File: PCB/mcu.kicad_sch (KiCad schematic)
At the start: 14 parts, among them SW1 SW_Push, SW2 SW_Push, SW3 SW_Push, SW4 SW_Push, U3 COM-09032, Y1 Crystal_GND24

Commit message: Fix wiring
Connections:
- new net: H1.2 (PA1), R10.2, SW2.2
- new net: H1.1 (PA0), R9.2, SW1.2
- new net: H1.3 (PA2), R11.2, SW3.2
- new net: H1.4 (PA3), R12.2, SW4.2
- now unconnected: H1.5 (PA4), H1.6 (PA5)
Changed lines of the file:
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@@
   (junction (at 88.9 158.75) (diameter 0) (color 0 0 0 0)
   )
-  (junction (at 68.58 74.93) (diameter 0) (color 0 0 0 0)
-  )
   (junction (at 49.53 74.93) (diameter 0) (color 0 0 0 0)
   )
@@
   (junction (at 68.58 130.81) (diameter 0) (color 0 0 0 0)
   )
-  (junction (at 68.58 80.01) (diameter 0) (color 0 0 0 0)
-  )
   (junction (at 45.72 72.39) (diameter 0) (color 0 0 0 0)
   )
@@
   (junction (at 95.25 170.18) (diameter 0) (color 0 0 0 0)
   )
-  (junction (at 68.58 72.39) (diameter 0) (color 0 0 0 0)
-  )
   (junction (at 57.15 80.01) (diameter 0) (color 0 0 0 0)
   )
@@
   (junction (at 49.53 60.96) (diameter 0) (color 0 0 0 0)
   )
-  (junction (at 68.58 82.55) (diameter 0) (color 0 0 0 0)
-  )
   (junction (at 93.98 52.07) (diameter 0) (color 0 0 0 0)
   )
@@
   )
   (junction (at 83.82 52.07) (diameter 0) (color 0 0 0 0)
-  )
-  (junction (at 68.58 77.47) (diameter 0) (color 0 0 0 0)
   )
   (junction (at 129.54 72.39) (diameter 0) (color 0 0 0 0)
@@
     (stroke (width 0) (type default))
   )
-  (wire (pts (xy 68.58 77.47) (xy 68.58 80.01))
-    (stroke (width 0) (type default))
-  )
   (wire (pts (xy 53.34 60.96) (xy 57.15 60.96))
     (stroke (width 0) (type default))
@@
     (stroke (width 0) (type default))
   )
-  (wire (pts (xy 68.58 80.01) (xy 68.58 82.55))
-    (stroke (width 0) (type default))
-  )
   (wire (pts (xy 53.34 77.47) (xy 48.26 77.47))
     (stroke (width 0) (type default))
@@
     (stroke (width 0) (type default))
   )
-  (wire (pts (xy 68.58 82.55) (xy 68.58 85.09))
-    (stroke (width 0) (type default))
-  )
-  (wire (pts (xy 68.58 72.39) (xy 68.58 74.93))
-    (stroke (width 0) (type default))
-  )
   (wire (pts (xy 104.14 52.07) (xy 106.68 52.07))
     (stroke (width 0) (type default))
@@
     (stroke (width 0) (type default))
   )
-  (wire (pts (xy 68.58 74.93) (xy 68.58 77.47))
-    (stroke (width 0) (type default))
-  )

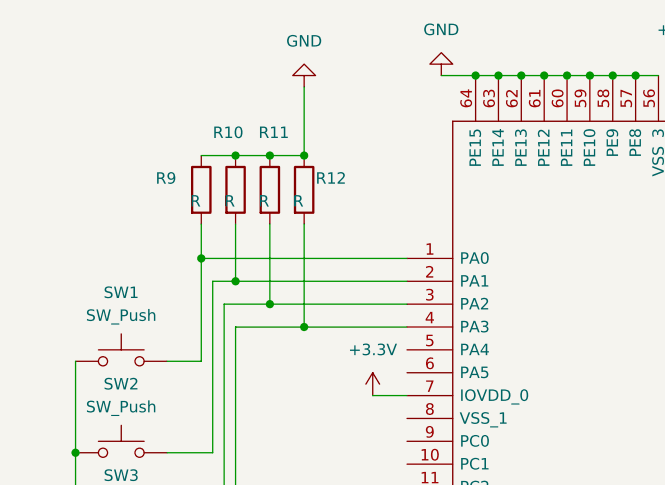
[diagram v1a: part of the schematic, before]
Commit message: Set resistor values
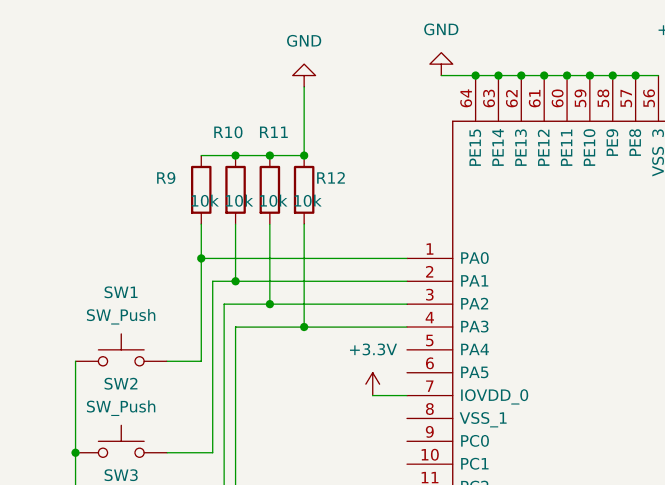
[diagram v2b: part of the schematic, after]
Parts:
- R10, R11, R12, R9: value R -> 10k
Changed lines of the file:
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@@
       (effects (font (size 1.27 1.27)) (justify left))
     )
-    (property "Value" "R" (at 48.26 66.04 0)
+    (property "Value" "10k" (at 48.26 66.04 0)
       (effects (font (size 1.27 1.27)) (justify left))
     )
@@
       (effects (font (size 1.27 1.27)) (justify left))
     )
-    (property "Value" "R" (at 44.45 66.04 0)
+    (property "Value" "10k" (at 44.45 66.04 0)
       (effects (font (size 1.27 1.27)) (justify left))
     )
@@
       (effects (font (size 1.27 1.27)) (justify left))
     )
-    (property "Value" "R" (at 55.88 66.04 0)
+    (property "Value" "10k" (at 55.88 66.04 0)
       (effects (font (size 1.27 1.27)) (justify left))
     )
@@
       (effects (font (size 1.27 1.27)) (justify left))
     )
-    (property "Value" "R" (at 52.07 66.04 0)
-      (effects (font (size 1.27 1.27)) (justify left))
-    )
+    (property "Value" "10k" (at 52.07 66.04 0)
+      (effects (font (size 1.27 1.27)) (justify left))
+    )

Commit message: Adding unit C and D to FPGA (Stil missing unit B)
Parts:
- H1: footprint QFP50P1200X1200X120-64N -> (none)
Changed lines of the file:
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@@
       (effects (font (size 1.27 1.27)))
     )
-    (property "Footprint" "QFP50P1200X1200X120-64N" (at 118.11 57.15 0)
+    (property "Footprint" "" (at 118.11 57.15 0)
       (effects (font (size 1.27 1.27)) (justify left) hide)
     )

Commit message: Work
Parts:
- added J3: USB_A, symbol Connector:USB_A
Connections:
- net GND: now also J3.4 (GND); no longer H1.47 (PF10), H1.48 (PF11)
- new net: H1.47 (PF10), J3.2 (D-)
- new net: H1.48 (PF11), J3.3 (D+)
- new net 5V_IN: J3.1 (VBUS)
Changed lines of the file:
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@@
   (junction (at 68.58 110.49) (diameter 0) (color 0 0 0 0)
   )
-  (junction (at 121.92 72.39) (diameter 0) (color 0 0 0 0)
-  )
   (junction (at 31.75 104.14) (diameter 0) (color 0 0 0 0)
   )
+  (junction (at 151.13 80.01) (diameter 0) (color 0 0 0 0)
+  )
   (junction (at 31.75 114.3) (diameter 0) (color 0 0 0 0)
   )
@@
   )
   (junction (at 83.82 52.07) (diameter 0) (color 0 0 0 0)
-  )
-  (junction (at 129.54 72.39) (diameter 0) (color 0 0 0 0)
   )
   (no_connect (at 123.19 77.47))
@@
     (stroke (width 0) (type default))
   )
+  (wire (pts (xy 151.13 80.01) (xy 158.75 80.01))
+    (stroke (width 0) (type default))
+  )
   (wire (pts (xy 57.15 80.01) (xy 49.53 80.01))
     (stroke (width 0) (type default))
   )
-  (wire (pts (xy 129.54 72.39) (xy 121.92 72.39))
-    (stroke (width 0) (type default))
-  )
-  (wire (pts (xy 129.54 72.39) (xy 158.75 72.39))
-    (stroke (width 0) (type default))
-  )
   (wire (pts (xy 31.75 93.98) (xy 31.75 83.82))
     (stroke (width 0) (type default))
@@
     (stroke (width 0) (type default))
   )
+  (wire (pts (xy 121.92 72.39) (xy 132.08 72.39))
+    (stroke (width 0) (type default))
+  )
   (wire (pts (xy 76.2 130.81) (xy 68.58 130.81))
     (stroke (width 0) (type default))
@@
     (stroke (width 0) (type default))
   )
+  (wire (pts (xy 132.08 72.39) (xy 132.08 66.04))
+    (stroke (width 0) (type default))
+  )
   (wire (pts (xy 95.25 171.45) (xy 95.25 170.18))
     (stroke (width 0) (type default))
   )
+  (wire (pts (xy 132.08 66.04) (xy 143.51 66.04))
+    (stroke (width 0) (type default))
+  )
   (wire (pts (xy 83.82 52.07) (xy 81.28 52.07))
     (stroke (width 0) (type default))
@@
     (stroke (width 0) (type default))
   )
+  (wire (pts (xy 151.13 76.2) (xy 151.13 80.01))
+    (stroke (width 0) (type default))
+  )
   (wire (pts (xy 49.53 68.58) (xy 49.53 74.93))
     (stroke (width 0) (type default))
@@
     (stroke (width 0) (type default))
   )
-  (wire (pts (xy 121.92 72.39) (xy 121.92 74.93))
-    (stroke (width 0) (type default))
-  )
   (wire (pts (xy 91.44 52.07) (xy 88.9 52.07))
     (stroke (width 0) (type default))
@@
     (stroke (width 0) (type default))
   )
+  (wire (pts (xy 138.43 60.96) (xy 143.51 60.96))
+    (stroke (width 0) (type default))
+  )
+  (wire (pts (xy 135.89 74.93) (xy 135.89 68.58))
+    (stroke (width 0) (type default))
+  )
   (wire (pts (xy 41.91 83.82) (xy 45.72 83.82))
     (stroke (width 0) (type default))
@@
     (stroke (width 0) (type default))
   )
-  (wire (pts (xy 121.92 80.01) (xy 129.54 80.01))
+  (wire (pts (xy 121.92 80.01) (xy 151.13 80.01))
     (stroke (width 0) (type default))
   )
@@
     (stroke (width 0) (type default))
   )
-  (wire (pts (xy 129.54 80.01) (xy 129.54 72.39))
-    (stroke (width 0) (type default))
-  )
   (wire (pts (xy 101.6 130.81) (xy 101.6 137.16))
     (stroke (width 0) (type default))
@@
     (stroke (width 0) (type default))
   )
+  (wire (pts (xy 121.92 74.93) (xy 135.89 74.93))
+    (stroke (width 0) (type default))
+  )
   (wire (pts (xy 57.15 68.58) (xy 57.15 80.01))
     (stroke (width 0) (type default))
@@
     (stroke (width 0) (type default))
   )
+  (wire (pts (xy 135.89 68.58) (xy 143.51 68.58))
+    (stroke (width 0) (type default))
+  )
   (wire (pts (xy 91.44 137.16) (xy 91.44 130.81))
     (stroke (width 0) (type default))
@@
   (wire (pts (xy 125.73 135.89) (xy 106.68 135.89))
     (stroke (width 0) (type default))
+  )
+  (hierarchical_label "5V_IN" (shape input) (at 138.43 60.96 180) (fields_autoplaced)
+    (effects (font (size 1.27 1.27)) (justify right))
   )
   (symbol (lib_id "power:GND") (at 104.14 52.07 0) (mirror x) (unit 1)
@@
     )
   )
-  (symbol (lib_id "power:GND") (at 158.75 72.39 90) (unit 1)
-    (in_bom yes) (on_board yes) (dnp no) (fields_autoplaced)
-    (property "Reference" "#PWR010" (at 165.1 72.39 0)
-      (effects (font (size 1.27 1.27)) hide)
-    )
-    (property "Value" "GND" (at 162.56 72.39 90)
+  (symbol (lib_id "power:GND") (at 158.75 80.01 90) (unit 1)
+    (in_bom yes) (on_board yes) (dnp no) (fields_autoplaced)
+    (property "Reference" "#PWR010" (at 165.1 80.01 0)
+      (effects (font (size 1.27 1.27)) hide)
+    )
+    (property "Value" "GND" (at 162.56 80.01 90)
       (effects (font (size 1.27 1.27)) (justify right))
     )
-    (property "Footprint" "" (at 158.75 72.39 0)
-      (effects (font (size 1.27 1.27)) hide)
-    )
-    (property "Datasheet" "" (at 158.75 72.39 0)
+    (property "Footprint" "" (at 158.75 80.01 0)
+      (effects (font (size 1.27 1.27)) hide)
+    )
+    (property "Datasheet" "" (at 158.75 80.01 0)
       (effects (font (size 1.27 1.27)) hide)
     )
@@
   )
   (symbol (lib_id "EFM32GG332F1024-QFP64:EFM32GG332F1024-QFP64") (at 68.58 72.39 0) (unit 1)
-    (in_bom yes) (on_board yes) (dnp no) (fields_autoplaced)
-    (property "Reference" "H1" (at 130.81 65.4619 0)
-      (effects (font (size 1.27 1.27)))
-    )
-    (property "Value" "EFM32GG332F1024-QFP64" (at 130.81 68.0019 0)
+    (in_bom yes) (on_board yes) (dnp no)
+    (property "Reference" "H1" (at 93.98 83.82 0)
+      (effects (font (size 1.27 1.27)))
+    )
+    (property "Value" "EFM32GG332F1024-QFP64" (at 96.52 86.36 0)
       (effects (font (size 1.27 1.27)))
     )
@@
         )
       )
+    )
+  )
+  (symbol (lib_id "Connector:USB_A") (at 151.13 66.04 0) (mirror y) (unit 1)
+    (in_bom yes) (on_board yes) (dnp no)
+    (property "Reference" "J3" (at 151.13 53.34 0)
+      (effects (font (size 1.27 1.27)))
+    )
+    (property "Value" "USB_A" (at 151.13 55.88 0)
+      (effects (font (size 1.27 1.27)))
+    )
+    (property "Footprint" "" (at 147.32 67.31 0)
+      (effects (font (size 1.27 1.27)) hide)
+    )
+    (property "Datasheet" " ~" (at 147.32 67.31 0)
+      (effects (font (size 1.27 1.27)) hide)
+    )
+    (pin "1")
+    (pin "2")
+    (pin "3")
+    (pin "4")
+    (pin "5")
+    (instances
+      (project "PCB"
+        (path "/aa113cd6-c3ac-4890-9a84-1ea195994408/6d6ebb76-19de-41e4-9a7d-528f4e5c1c0f"
+          (reference "J3") (unit 1)
+        )
+      )

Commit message: more work
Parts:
- added JTAG_DEBUG: FTSH-110-01-L-DV-007, FTSH-110-01-L-DV-007:SAMTEC_FTSH-110-01-L-DV-007, symbol FTSH-110-01-L-DV-007:FTSH-110-01-L-DV-007
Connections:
- net GND: no longer H1.15 (PB7), H1.16 (PB8)
- net MISO: now reaches H1.10 (PC1)
- net MOSI: now reaches H1.11 (PC2)
- new net CLK: H1.15 (PB7)
- new net CS: H1.16 (PB8)
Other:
- moved on the sheet: SW1, SW2, SW3, SW4

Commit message: work
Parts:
- C22: value C -> 1u
- renumbered JTAG_DEBUG to DEBUG_HEADER
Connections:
- net +3.3V: now also DEBUG_HEADER.01 (VCC)
- net GND: now also DEBUG_HEADER.03 (GND), DEBUG_HEADER.05 (GND), DEBUG_HEADER.09 (GNDDetect), DEBUG_HEADER.11 (GND), DEBUG_HEADER.13 (GND), DEBUG_HEADER.15 (GND), DEBUG_HEADER.17 (GND), DEBUG_HEADER.19 (GND), H1.12 (PC3), H1.13 (PC4), H1.14 (PC5), H1.30 (PD2), H1.36 (PD8), H1.37 (PC6), H1.38 (PC7), H1.41 (PC8), H1.42 (PC9), H1.43 (PC10), H1.44 (PC11), H1.5 (PA4), H1.54 (PF5), H1.6 (PA5), H1.8 (VSS_1), H1.9 (PC0); no longer H1.57 (PE8), H1.58 (PE9), H1.59 (PE10), H1.60 (PE11), H1.61 (PE12), H1.62 (PE13), H1.63 (PE14), H1.64 (PE15)
- net at DEBUG_HEADER.02 (SWDIO): now also H1.50 (PF1)
- net at DEBUG_HEADER.04 (SWDCLK): now also H1.49 (PF0)
- net at DEBUG_HEADER.06 (SWO): now also H1.51 (PF2)
- net at DEBUG_HEADER.08 (nRESET): now also H1.20 (RESETN)
- net at DEBUG_HEADER.12 (TRACECLK): now also H1.35 (PD7)
- net at DEBUG_HEADER.14 (TRACEDATA[0]): now also H1.34 (PD6)
- net at DEBUG_HEADER.16 (TRACEDATA[1]): now also H1.31 (PD3)
- net at DEBUG_HEADER.18 (TRACEDATA[2]): now also H1.32 (PD4)
- net at DEBUG_HEADER.20 (TRACEDATA[3]): now also H1.33 (PD5)
- new net GPIO0: H1.64 (PE15)
- new net GPIO1: H1.63 (PE14)
- new net GPIO2: H1.62 (PE13)
- new net GPIO3: H1.61 (PE12)
- new net GPIO4: H1.60 (PE11)
- new net GPIO5: H1.59 (PE10)
- new net GPIO6: H1.58 (PE9)
- new net GPIO7: H1.57 (PE8)
- no-connect marks 1 -> 6
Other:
- moved on the sheet: DEBUG_HEADER, U3

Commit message: Add
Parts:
- C20, C21: value C -> 12p
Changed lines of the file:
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@@
       (effects (font (size 1.27 1.27)) (justify left))
     )
-    (property "Value" "C" (at 92.71 167.64 0)
+    (property "Value" "12p" (at 92.71 167.64 0)
       (effects (font (size 1.27 1.27)) (justify left))
     )
@@
       (effects (font (size 1.27 1.27)) (justify left))
     )
-    (property "Value" "C" (at 105.41 167.64 0)
+    (property "Value" "12p" (at 105.41 167.64 0)
       (effects (font (size 1.27 1.27)) (justify left))
     )
